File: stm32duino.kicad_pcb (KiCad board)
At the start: 2 copper layers, 87.6 x 48.3 mm, 20 parts, among them P1 RF7021SE, P2 DISP_I2C, P3 DISP_SER, P4 HOST_SER, U1 stm32f103c8t6-module-china

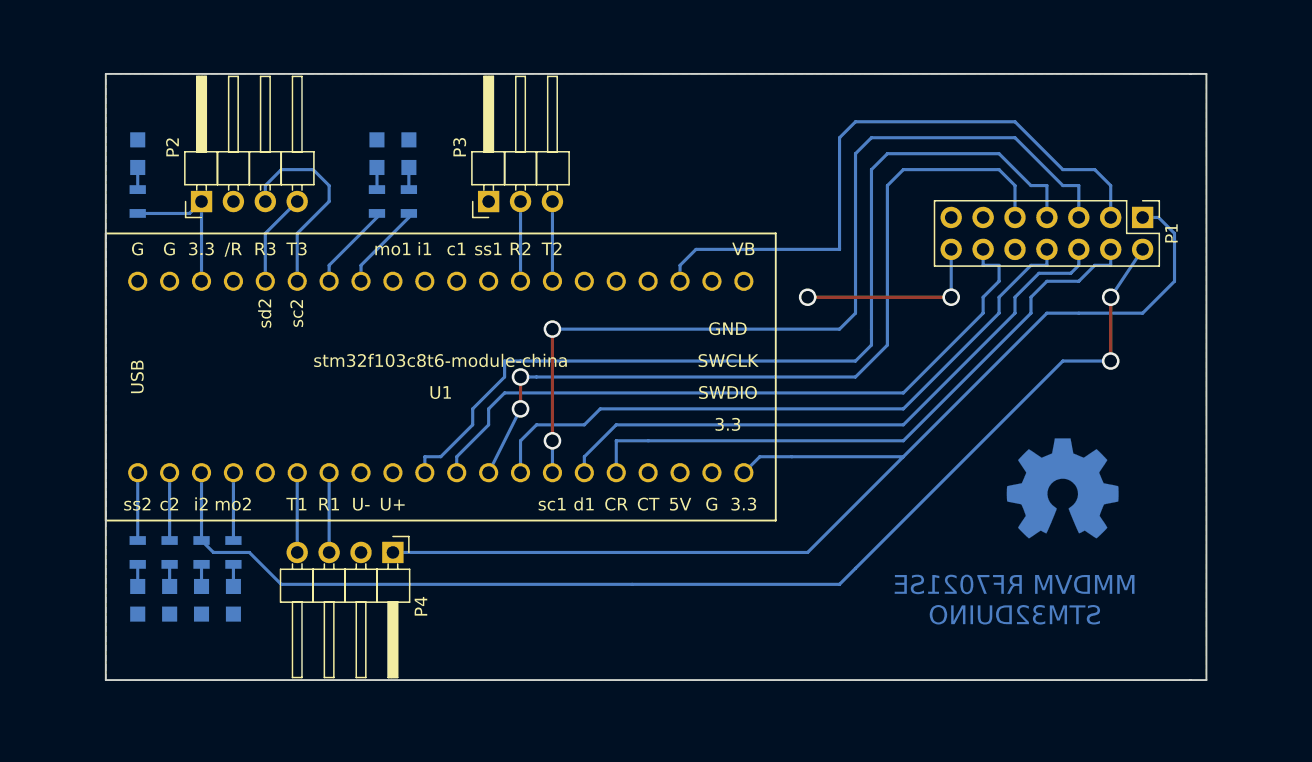
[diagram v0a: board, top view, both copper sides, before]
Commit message: modified for Trhuhole components, added NXD LED.
Modifications from original Project:
-Changed LEDs and resistors from SMD to TrhuHole, and facing to the front of the board.
-Added LED for NXD operation.
-Increased track width for RF7021SE +3.3 VDC.
-Modified header connectors orientation for 3D view.
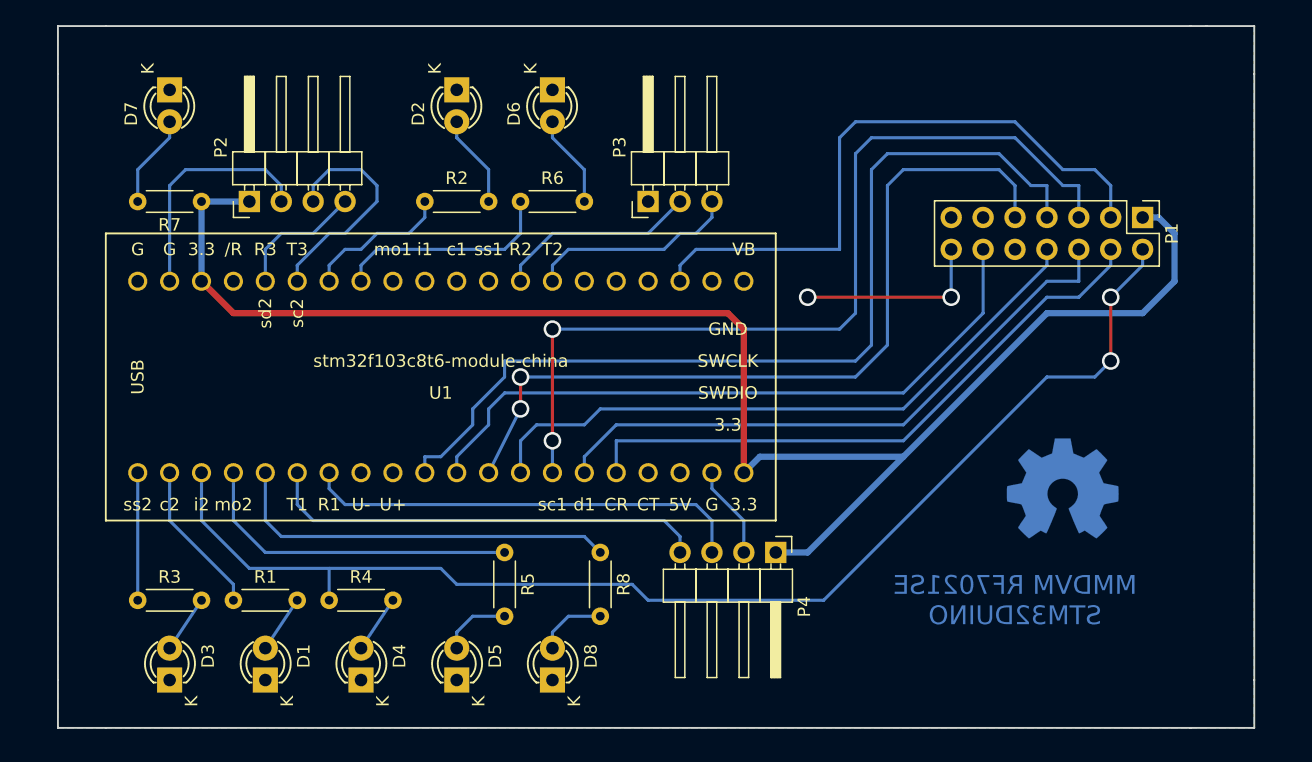
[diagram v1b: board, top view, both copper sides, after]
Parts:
- added D8: LED, LEDs:LED-3MM, F.Cu at (135.9, 83.8)
- added R8: 1K5, Resistors_THT:R_Axial_DIN0204_L3.6mm_D1.6mm_P5.08mm_Horizontal, F.Cu at (139.7, 73.7)
- D1, D2, D3, D4, D5, D6, D7: footprint LEDs:LED_0805 -> LEDs:LED-3MM; moved to F.Cu
- R1, R2, R3, R4, R5, R6, R7: footprint Resistors_SMD:R_0805 -> Resistors_THT:R_Axial_DIN0204_L3.6mm_D1.6mm_P5.08mm_Horizontal; moved to F.Cu
- moved P4 30.5 mm to (153.7, 73.7)
- moved R5 21.6 mm to (132.1, 73.7)
- moved D5 18.9 mm to (128.3, 83.8)
- moved D4 14.2 mm to (120.7, 83.8)
- moved P3 12.7 mm to (143.5, 45.7)
- moved D6 12.5 mm to (135.9, 36.8)
- moved R4 10.9 mm to (118.1, 77.5), turned to 0 degrees
- moved D1 9.92 mm to (113.0, 83.8)
- moved R6 8.89 mm to (133.3, 45.7), turned to 0 degrees
- moved D2 8.13 mm to (128.3, 36.8)
- moved D3 6.84 mm to (105.4, 83.8)
- moved R1 6.35 mm to (110.5, 77.5), turned to 0 degrees
- moved D7 5.68 mm to (105.4, 36.8)
- moved R7 5.08 mm to (108.0, 45.7), turned to 180 degrees
- moved P2 3.81 mm to (111.8, 45.7)
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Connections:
- U1 pad 5: Net-(U1-Pad5) -> LEDNXD
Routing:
- net LEDNXD: track 0.00 -> 31.5 mm
- net HOST_TX: track 6.35 -> 35.3 mm
- net HOST_RX: track 6.35 -> 35.3 mm
- net GND: track 15.2 -> 41.5 mm
- net +3V3: track 103.1 -> 127.1 mm
- net LED_COS: track 5.40 -> 26.5 mm
- net LEDP25: track 6.98 -> 17.6 mm
- net DISP_TX: track 6.35 -> 16.8 mm
- net DISP_RX: track 6.35 -> 16.1 mm
- net LEDDMR: track 5.40 -> 12.3 mm
- net Net-(D6-Pad2): track 1.76 -> 7.40 mm
- net Net-(D7-Pad2): track 1.76 -> 7.40 mm
- net Net-(D2-Pad2): track 1.76 -> 7.40 mm
- net Net-(D8-Pad2): track 0.00 -> 5.61 mm
- net LEDDSTAR: track 5.40 -> 10.2 mm
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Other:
- board size 87.6 x 48.3 mm -> 95.3 x 55.9 mm
- net class power added: clearance 0.2, trace_width 0.5, via_dia 1.4, via_drill 1

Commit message: Added Mounting holes and RF7021 breakout board footprint
Additions: 3.5mm mounting holes on corners., footprint for RF7021 breakout board, Text labels for CC licensing, model, usage and credits, text labels for LED indicator signals.
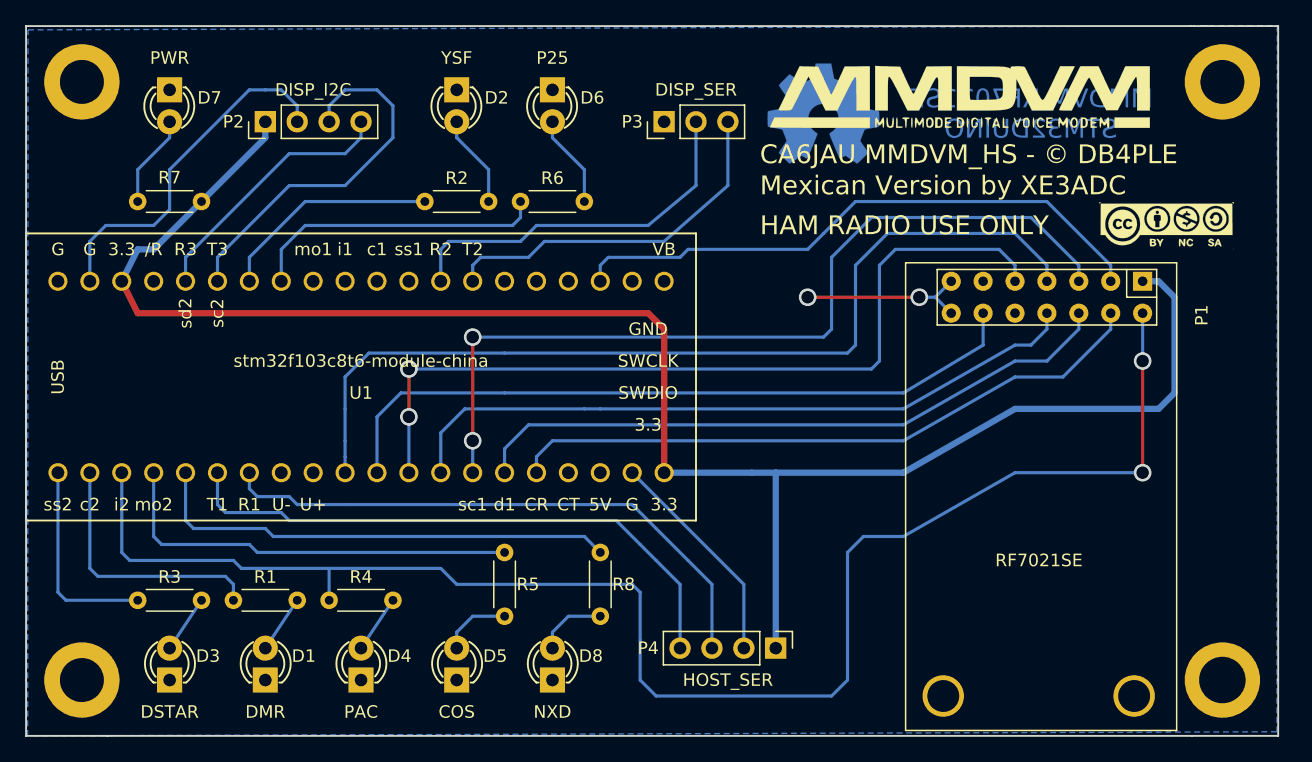
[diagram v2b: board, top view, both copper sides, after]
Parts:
- added G***: LOGO, Graphic:MMDVM, F.Cu at (168.3, 37.5)
- added G***: LOGO, Graphic:CC, F.Cu at (184.8, 47.6)
- added MH1: D=3.5mm, Mounting_Holes:MountingHole_3.5mm_Pad, F.Cu at (98.4, 36.2)
- added MH2: D=3.5mm, Mounting_Holes:MountingHole_3.5mm_Pad, F.Cu at (189.2, 36.2)
- added MH3: D=3.5mm, Mounting_Holes:MountingHole_3.5mm_Pad, F.Cu at (98.4, 83.8)
- added MH4: D=3.5mm, Mounting_Holes:MountingHole_3.7mm_Pad, F.Cu at (189.2, 83.8)
- ?: renamed from REF***; value OSHW-Symbol_8.9x8mm_Copper -> (none)
- D1: value LED -> DMR
- D2: value LED -> YSF
- D3: value LED -> DSTAR
- D4: value LED -> PAC
- D5: value LED -> COS
- D6: value LED -> P25
- D7: value LED -> PWR
- D8: value LED -> NXD
- P1: footprint Pin_Headers:Pin_Header_Straight_2x07_Pitch2.54mm -> RF_Modules:RF7021SE_Breakout
- P2, P4: footprint Pin_Headers:Pin_Header_Angled_1x04_Pitch2.54mm -> Pin_Headers:Pin_Header_Straight_1x04_Pitch2.54mm
- P3: footprint Pin_Headers:Pin_Header_Angled_1x03_Pitch2.54mm -> Pin_Headers:Pin_Header_Straight_1x03_Pitch2.54mm
- moved ? 35.4 mm to (157.5, 38.7)
- moved P4 7.62 mm to (153.7, 81.3)
- moved P3 6.48 mm to (144.8, 39.4)
- moved P2 6.48 mm to (113.0, 39.4)
- moved U1 6.35 mm to (120.7, 59.7)
- moved P1 5.08 mm to (182.9, 52.1)
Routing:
- net PAC: track 99.2 -> 124.3 mm
- net GND: track 41.5 -> 59.7 mm
- net +3V3: track 127.1 -> 141.8 mm
- net DISP_RX: track 16.1 -> 29.9 mm
- net DISP_TX: track 16.8 -> 29.1 mm
- net HOST_TX: track 35.3 -> 47.1 mm
- net Net-(P2-Pad3): track 18.4 -> 29.8 mm
- net HOST_RX: track 35.3 -> 46.3 mm
- net Net-(P2-Pad4): track 10.5 -> 21.1 mm
- net LEDDMR: track 12.3 -> 20.8 mm
- net LED_COS: track 26.5 -> 33.5 mm
- net LEDP25: track 17.6 -> 23.9 mm
- net LEDNXD: track 31.5 -> 37.9 mm
- net LEDDSTAR: track 10.2 -> 16.1 mm
- net LEDYSF: track 11.7 -> 17.7 mm
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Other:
- board size 95.3 x 55.9 mm -> 99.7 x 56.5 mm
- board text added: "CA6JAU MMDVM_HS - © DB4PLE"
- board text added: "HAM RADIO USE ONLY"
- board text added: "Mexican Version by XE3ADC"
